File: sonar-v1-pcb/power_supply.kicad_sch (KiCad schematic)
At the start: 30 parts, among them SW2901 SW_SPDT, U2901 TPS7A2033DQN, U2902 TPS7A2028DQN, U2903 TPS62912, U2904 TPS7A205DQN, U2905 TPS7A91, U2906 LM337IMPX-TP

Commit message: Some work on the boost converter
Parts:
- removed U2906: LM337IMPX-TP, Sonar:SOT-223, symbol sonar_lib:LM337IMPX-TP
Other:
- sheet 12V_to_10V_LDO renamed 12V to 10V LDO
- sheet 5V_to_12V_boost renamed Vin to 12V Boost
- added sheet -10V Negative LDO (-10v_negative_ldo.kicad_sch)
- note removed: "??? inverting buck boost"
- title: (none) -> Power
- moved on the sheet: R2901

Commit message: some stuff i forget
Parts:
- added TP2903: -12V, symbol Connector:TestPoint_Probe
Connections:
- net -12V: now also TP2903.1
- net 5v_12v_boost/12V: no longer names the net of C2910.1, C2911.1, C2912.1, C2913.1, U2903.1 (EN/SYNC), U2903.10 (S-CONF), U2903.6 (VIN)
- net 5v_12v_boost/GND: no longer names the net of SW2901.1 (A)
- net 5v_12v_boost/enable: no longer names the net of SW2901.2 (B)
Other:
- removed sheet 5v_12v_boost
- sheet Vin to 12V Boost ports: added GND, Vin, Vout; removed none
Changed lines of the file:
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@@
 	)
 	(junction
+		(at 208.28 177.8)
+		(diameter 0)
+		(color 0 0 0 0)
+	)
+	(junction
 		(at 651.51 81.28)
 		(diameter 0)
@@
 	(wire
 		(pts
+			(xy 208.28 177.8) (xy 222.25 177.8)
+		)
+		(stroke
+			(width 0)
+			(type default)
+		)
+	)
+	(wire
+		(pts
 			(xy 626.11 91.44) (xy 638.81 91.44)
 		)
@@
 	(wire
 		(pts
-			(xy 194.31 177.8) (xy 220.98 177.8)
+			(xy 194.31 177.8) (xy 208.28 177.8)
 		)
 		(stroke
@@
 	(wire
 		(pts
-			(xy 260.35 177.8) (xy 254 177.8)
+			(xy 261.62 177.8) (xy 255.27 177.8)
 		)
 		(stroke
@@
 	)
 	(label "-10V"
-		(at 260.35 177.8 180)
+		(at 261.62 177.8 180)
 		(effects
 			(font
@@
 	)
 	(label "-12V"
-		(at 214.63 177.8 0)
+		(at 215.9 177.8 0)
 		(effects
 			(font
@@
 	)
 	(symbol
+		(lib_id "Connector:TestPoint_Probe")
+		(at 208.28 177.8 0)
+		(unit 1)
+		(exclude_from_sim no)
+		(in_bom yes)
+		(on_board yes)
+		(dnp no)
+		(property "Reference" "TP2903"
+			(at 209.55 170.18 0)
+			(effects
+				(font
+					(size 1.27 1.27)
+				)
+			)
+		)
+		(property "Value" "-12V"
+			(at 209.55 172.72 0)
+			(effects
+				(font
+					(size 1.27 1.27)
+				)
+			)
+		)
+		(property "Footprint" ""
+			(at 213.36 177.8 0)
+			(effects
+				(font
+					(size 1.27 1.27)
+				)
+				(hide yes)
+			)
+		)
+		(property "Datasheet" "~"
+			(at 213.36 177.8 0)
+			(effects
+				(font
+					(size 1.27 1.27)
+				)
+				(hide yes)
+			)
+		)
+		(property "Description" "test point (alternative probe-style design)"
+			(at 208.28 177.8 0)
+			(effects
+				(font
+					(size 1.27 1.27)
+				)
+				(hide yes)
+			)
+		)
+		(pin "1"
+		)
+		(instances
+			(project "sonar"
+				(path "/f72ceae0-eee4-4385-b0e8-639846bcb5f2/0971c334-b681-41ae-ad35-a89520df0687"
+					(reference "TP2903")
+					(unit 1)
+				)
+			)
+		)
+	)
+	(symbol
 		(lib_id "Device:C")
 		(at 651.51 86.36 0)
@@
 	)
 	(sheet
-		(at 161.29 71.12)
-		(size 30.48 22.86)
+		(at 160.02 71.12)
+		(size 34.29 22.86)
 		(exclude_from_sim no)
 		(in_bom yes)
@@
 		)
 		(property "Sheetname" "Vin to 12V Boost"
-			(at 161.29 70.4084 0)
+			(at 160.02 70.4084 0)
 			(effects
 				(font
@@
 		)
 		(property "Sheetfile" "5v_to_12v_boost.kicad_sch"
-			(at 161.29 94.5646 0)
-			(effects
-				(font
-					(size 1.27 1.27)
-				)
-				(justify left top)
-			)
-		)
-		(instances
-			(project "sonar"
-				(path "/f72ceae0-eee4-4385-b0e8-639846bcb5f2/0971c334-b681-41ae-ad35-a89520df0687"
-					(page "33")
-				)
-			)
-		)
-	)
-	(sheet
-		(at 502.92 91.44)
-		(size 27.94 26.67)
-		(exclude_from_sim no)
-		(in_bom yes)
-		(on_board yes)
-		(dnp no)
-		(fields_autoplaced yes)
-		(stroke
-			(width 0.1524)
-			(type solid)
-		)
-		(fill
-			(color 0 0 0 0.0000)
-		)
-		(property "Sheetname" "5v_12v_boost"
-			(at 502.92 90.7284 0)
-			(effects
-				(font
-					(size 1.27 1.27)
-				)
-				(justify left bottom)
-			)
-		)
-		(property "Sheetfile" "5_to_10_boost.kicad_sch"
-			(at 502.92 118.6946 0)
+			(at 160.02 94.5646 0)
 			(effects
 				(font
@@
 		)
 		(pin "GND" input
-			(at 502.92 113.03 180)
+			(at 160.02 90.17 180)
 			(effects
 				(font
@@
 			)
 		)
-		(pin "enable" input
-			(at 502.92 105.41 180)
-			(effects
-				(font
-					(size 1.27 1.27)
-				)
-				(justify left)
-			)
-		)
-		(pin "VBUS" input
-			(at 502.92 96.52 180)
+		(pin "Vin" input
+			(at 160.02 74.93 180)
 			(effects
 				(font
@@
 			)
 		)
-		(pin "12V" output
-			(at 530.86 101.6 0)
+		(pin "Vout" output
+			(at 194.31 74.93 0)
 			(effects
 				(font
@@
 			(project "sonar"
 				(path "/f72ceae0-eee4-4385-b0e8-639846bcb5f2/0971c334-b681-41ae-ad35-a89520df0687"
-					(page "31")
+					(page "33")
 				)
 			)
@@
 	)
 	(sheet
-		(at 220.98 171.45)
-		(size 33.02 24.13)
+		(at 222.25 172.72)
+		(size 33.02 22.86)
 		(exclude_from_sim no)
 		(in_bom yes)
@@
 		)
 		(property "Sheetname" "-10V Negative LDO"
-			(at 220.98 170.7384 0)
+			(at 222.25 172.0084 0)
 			(effects
 				(font
@@
 		)
 		(property "Sheetfile" "-10v_negative_ldo.kicad_sch"
-			(at 220.98 196.1646 0)
+			(at 222.25 196.1646 0)
 			(effects
 				(font
@@
 		)
 		(pin "GND" input
-			(at 220.98 191.77 180)
+			(at 222.25 191.77 180)
 			(effects
 				(font
@@
 		)
 		(pin "Vin" input
-			(at 220.98 177.8 180)
+			(at 222.25 177.8 180)
 			(effects
 				(font
@@
 		)
 		(pin "Vout" output
-			(at 254 177.8 0)
+			(at 255.27 177.8 0)
 			(effects
 				(font
@@
 	)
 	(sheet
-		(at 160.02 171.45)
-		(size 34.29 24.13)
+		(at 160.02 172.72)
+		(size 34.29 22.86)
 		(exclude_from_sim no)
 		(in_bom yes)
@@
 		)
 		(property "Sheetname" "Vin to -12V Inverting Buck Boost"
-			(at 160.02 170.7384 0)
+			(at 160.02 172.0084 0)
 			(effects
 				(font
@@
 	)
 	(sheet
-		(at 213.36 71.12)
-		(size 25.4 22.86)
+		(at 222.25 71.12)
+		(size 33.02 22.86)
 		(exclude_from_sim no)
 		(in_bom yes)
@@
 		)
 		(property "Sheetname" "12V to 10V LDO"
-			(at 213.36 70.4084 0)
+			(at 222.25 70.4084 0)
 			(effects
 				(font
@@
 		)
 		(property "Sheetfile" "12v_to_10v_ldo.kicad_sch"
-			(at 213.36 94.5646 0)
+			(at 222.25 94.5646 0)
 			(effects
 				(font

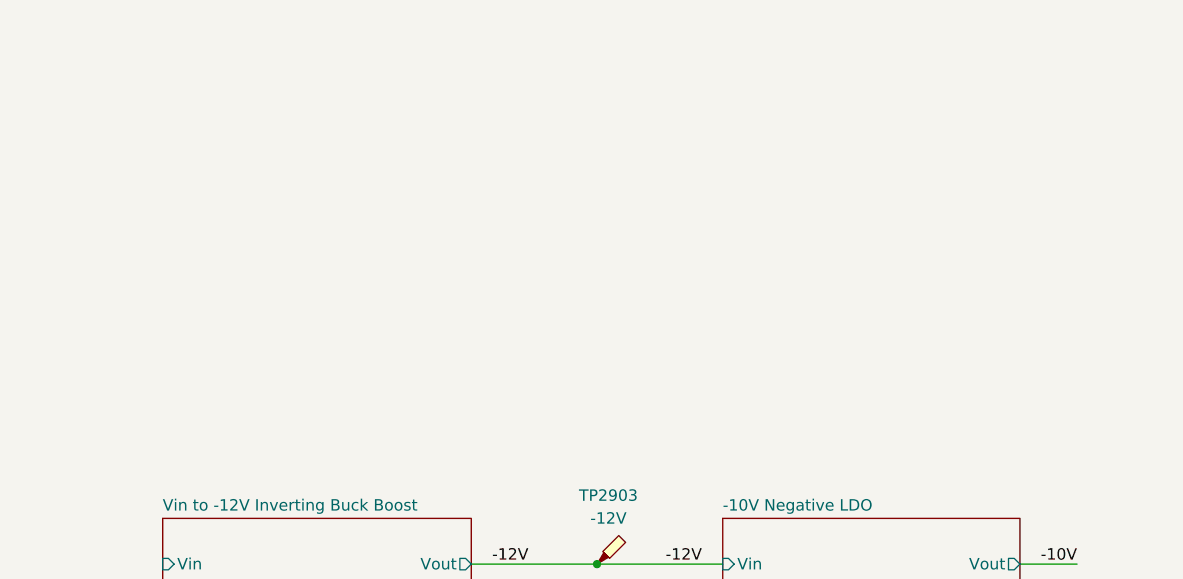
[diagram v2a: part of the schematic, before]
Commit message: Update to v10 and add an LDO
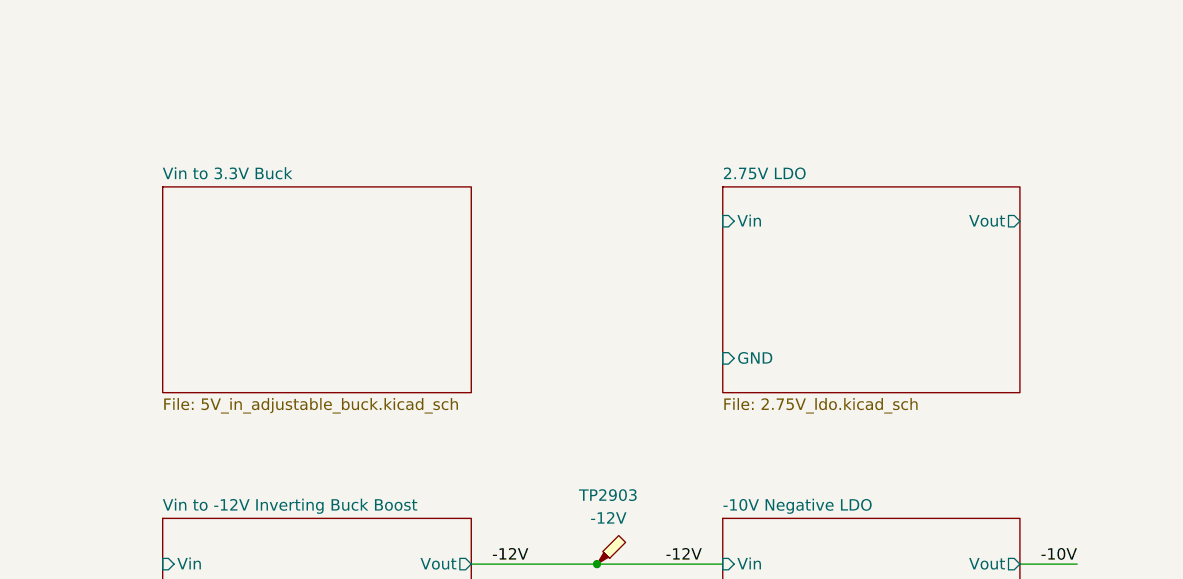
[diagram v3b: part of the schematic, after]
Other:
- added sheet 2.75V LDO (2.75V_ldo.kicad_sch)
- added sheet Vin to 3.3V Buck (5V_in_adjustable_buck.kicad_sch)

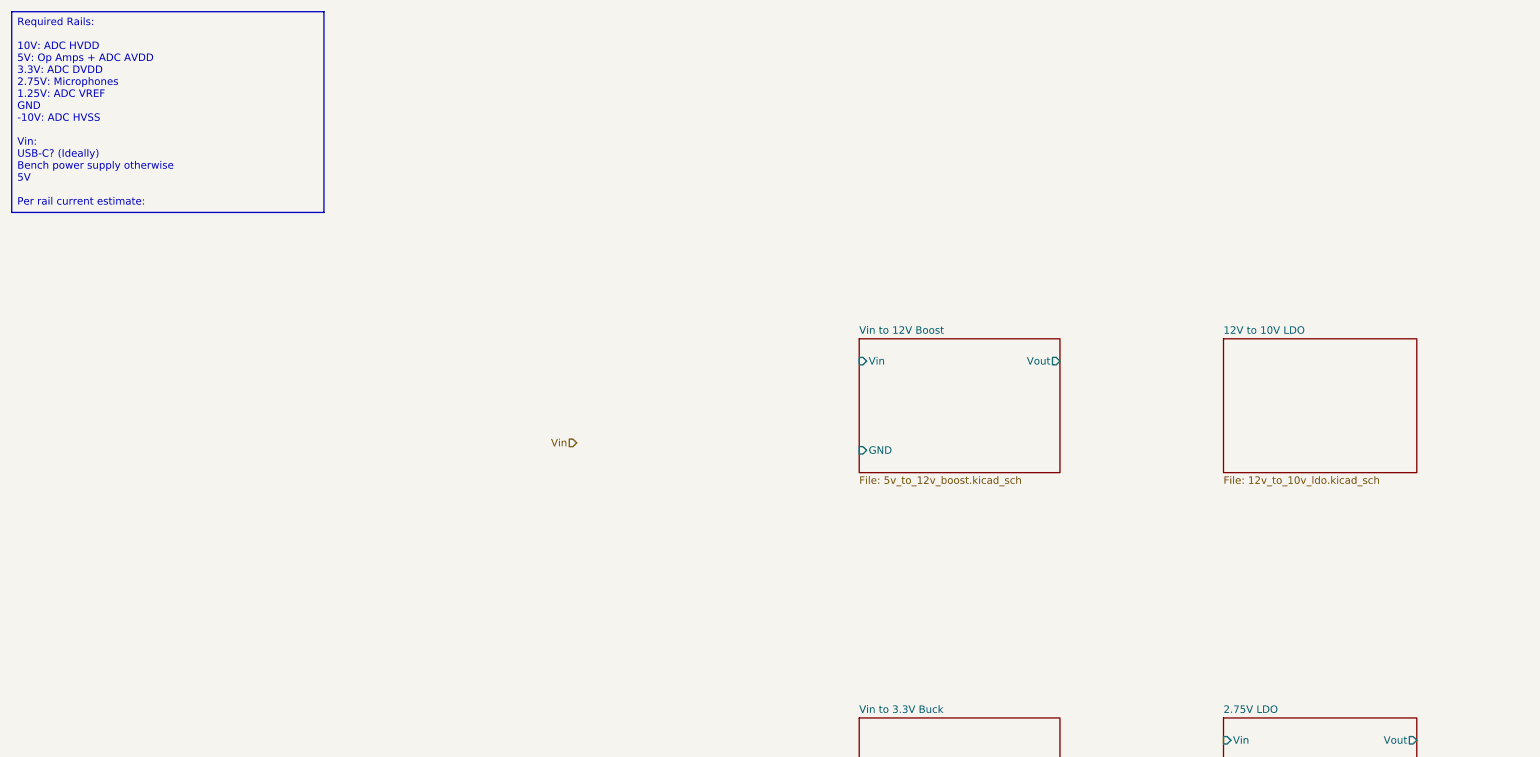
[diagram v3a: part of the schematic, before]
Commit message: Add an h-bridge
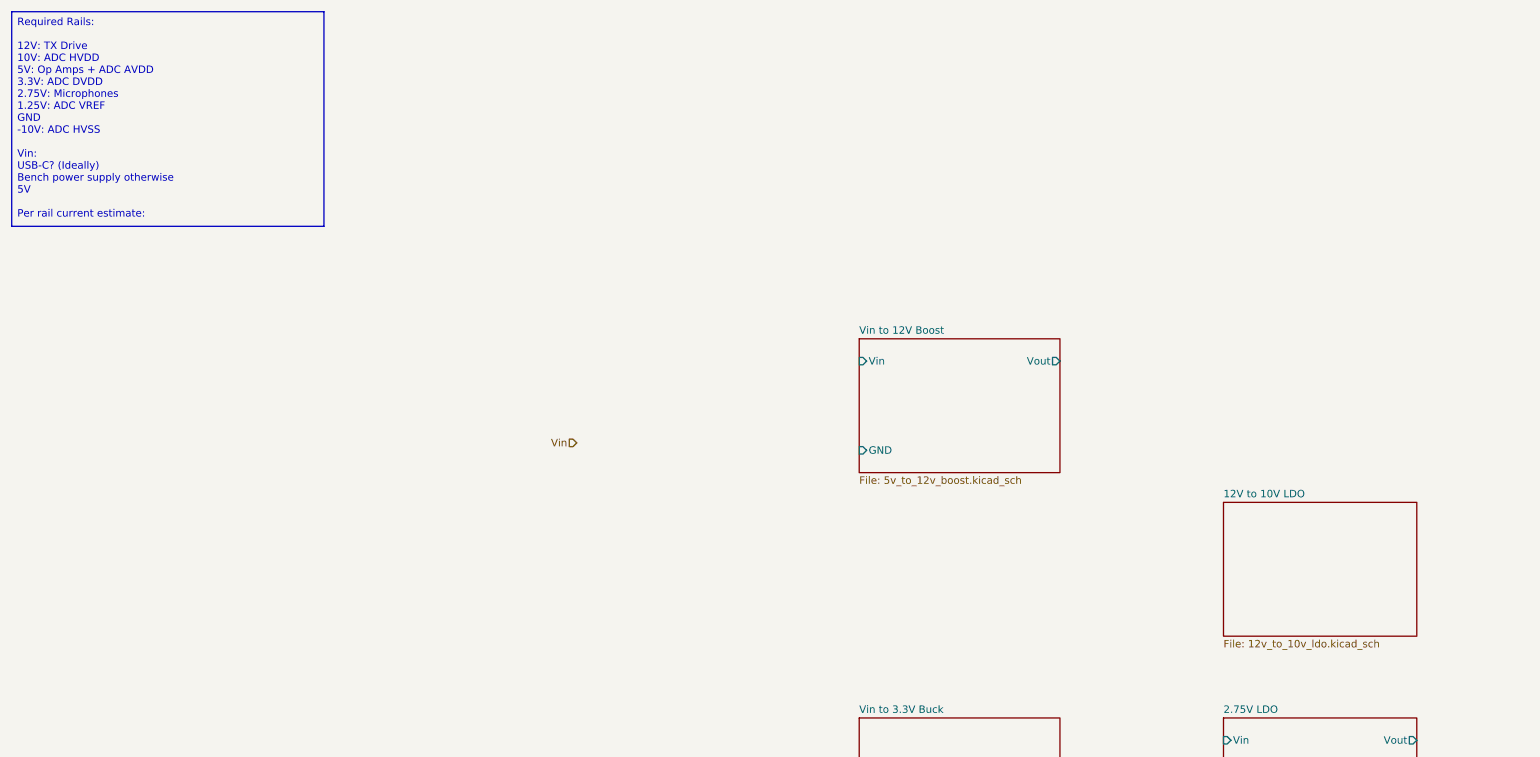
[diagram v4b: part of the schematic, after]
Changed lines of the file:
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@@
 		)
 	)
-	(text_box "Required Rails:\n\n10V: ADC HVDD\n5V: Op Amps + ADC AVDD\n3.3V: ADC DVDD\n2.75V: Microphones\n1.25V: ADC VREF\nGND\n-10V: ADC HVSS\n\nVin:\nUSB-C? (Ideally)\nBench power supply otherwise\n5V\n\nPer rail current estimate:\n"
+	(text_box "Required Rails:\n\n12V: TX Drive\n10V: ADC HVDD\n5V: Op Amps + ADC AVDD\n3.3V: ADC DVDD\n2.75V: Microphones\n1.25V: ADC VREF\nGND\n-10V: ADC HVSS\n\nVin:\nUSB-C? (Ideally)\nBench power supply otherwise\n5V\n\nPer rail current estimate:\n"
 		(exclude_from_sim no)
 		(at 15.24 15.24 0)
-		(size 53.34 34.29)
+		(size 53.34 36.6624)
 		(margins 0.9525 0.9525 0.9525 0.9525)
 		(stroke
@@
 	)
 	(sheet
-		(at 222.25 71.12)
+		(at 222.25 99.06)
 		(size 33.02 22.86)
 		(exclude_from_sim no)
@@
 		)
 		(property "Sheetname" "12V to 10V LDO"
-			(at 222.25 70.4084 0)
+			(at 222.25 98.3484 0)
 			(show_name no)
 			(do_not_autoplace no)
@@
 		)
 		(property "Sheetfile" "12v_to_10v_ldo.kicad_sch"
-			(at 222.25 94.5646 0)
+			(at 222.25 122.5046 0)
 			(show_name no)
 			(do_not_autoplace no)
